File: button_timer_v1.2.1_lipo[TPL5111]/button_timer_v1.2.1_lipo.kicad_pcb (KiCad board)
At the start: 2 copper layers, 21 x 41.7 mm, 23 parts, among them J1 Conn_01x05_Female, SW1 SW_Push, SW2 SW_Push, U2 AP2112K-3.3, U3 TPL5111, X1 ESP-12E

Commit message: 3D Models etwas verbessert
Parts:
- C5: footprint Capacitor_SMD:C_0805_2012Metric_Pad1.18x1.45mm_HandSolder -> handsolder:C_0402_1005Metric_Pad0.74x0.62mm_HandSoldermod
- J1: footprint Connector_PinHeader_2.54mm:PinHeader_1x05_P2.54mm_Vertical -> Connector_PinSocket_2.54mm:PinSocket_1x05_P2.54mm_Vertical
- SW1: footprint Button_Switch_THT:SW_PUSH_6mm -> Button_Switch_THT:SW_PUSH_6mm_H8mm
- SW2: footprint Button_Switch_SMD:SW_SPST_EVQPE1 -> Button_Switch_SMD:SW_SPST_B3U-1000P
- moved C5 0.23 mm to (123.2, 64.0)
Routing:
- net Net-(BT1-Pad1): track 26.7 -> 18.7 mm
- net /GND: track 96.8 -> 97.4 mm

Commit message: Silkscreen Update
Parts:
- D2: footprint LED_SMD:LED_0805_2012Metric_Castellated -> handsolder:LED_0805_2012Metric_Castellated_mod

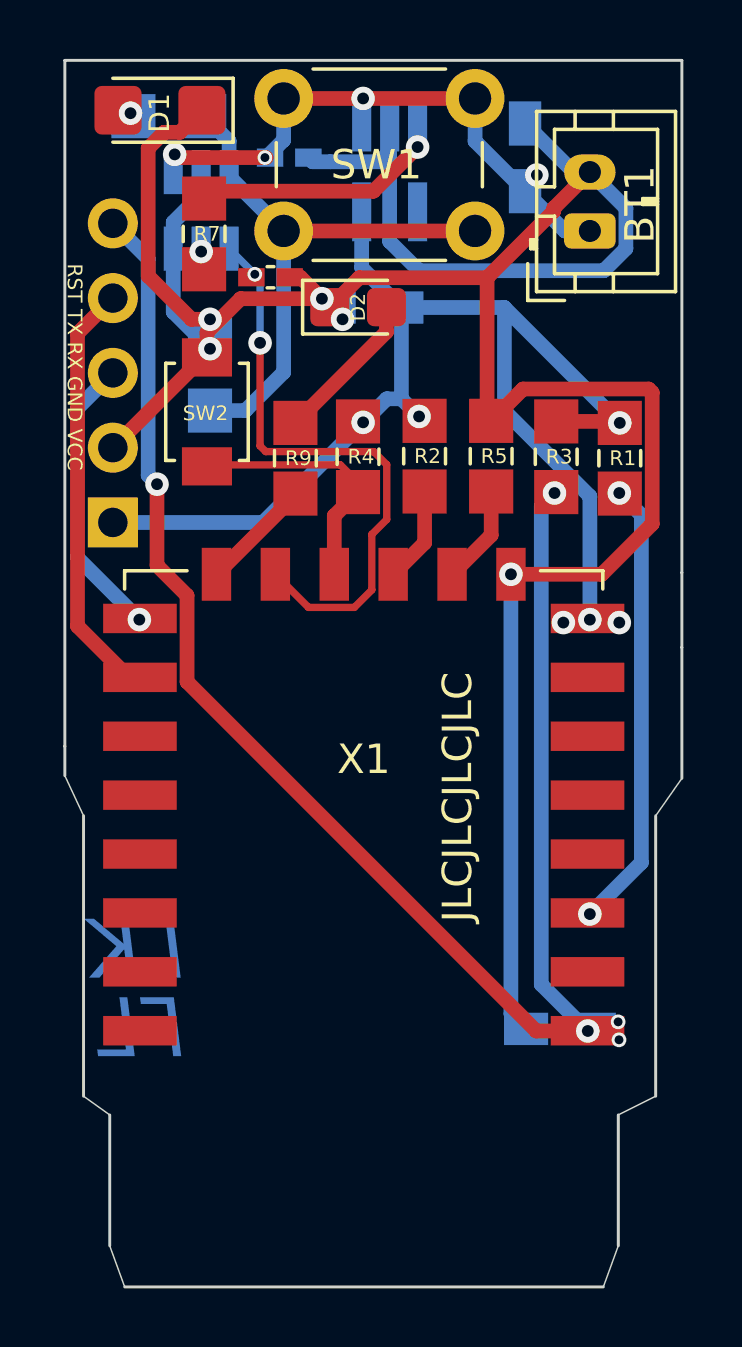
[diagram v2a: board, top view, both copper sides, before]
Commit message: cap between esp vcc and ground added
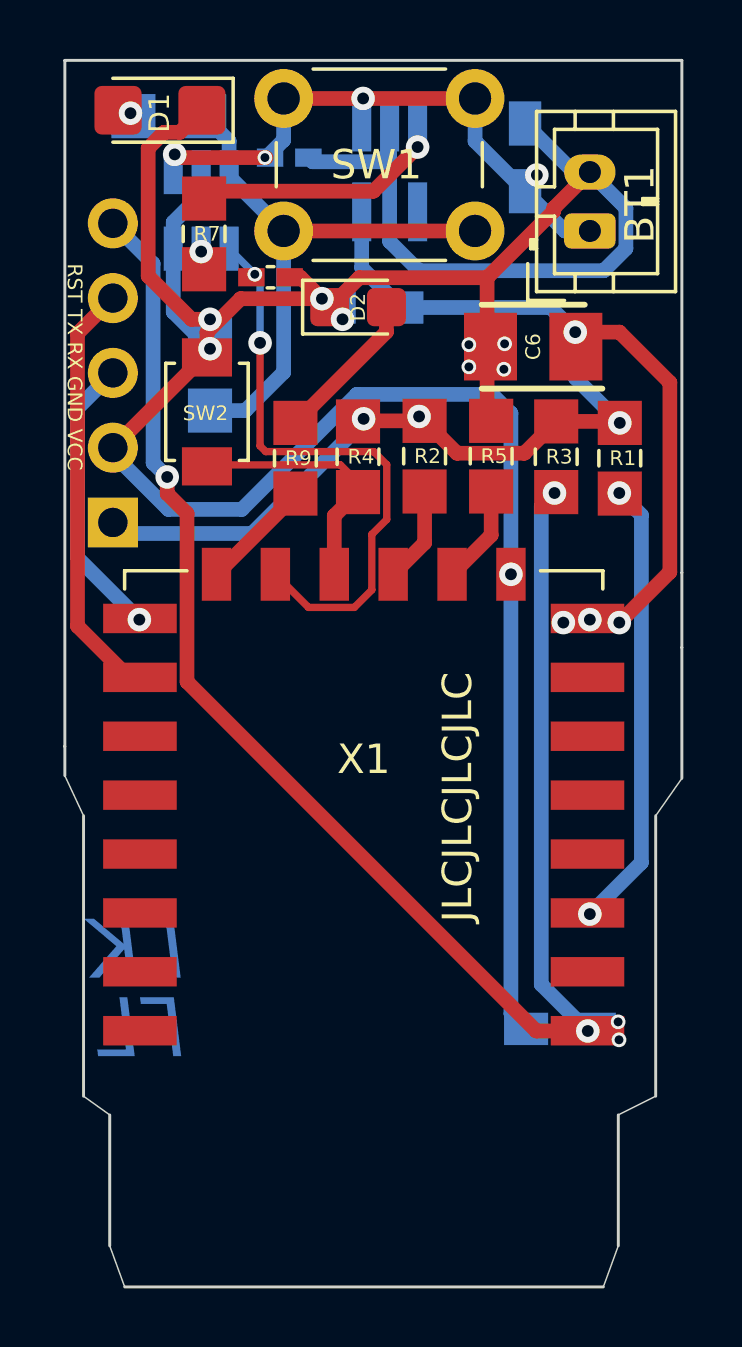
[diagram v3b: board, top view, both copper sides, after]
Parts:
- added C6: TAJB476M010TNJ, SamacSys_Parts:CAPPM3528X210N, F.Cu at (131.5, 70.4)
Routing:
- net /GND: track 97.4 -> 103.3 mm, vias 5 -> 9
- net /VCC: track 42.3 -> 46.5 mm, vias 6 -> 7

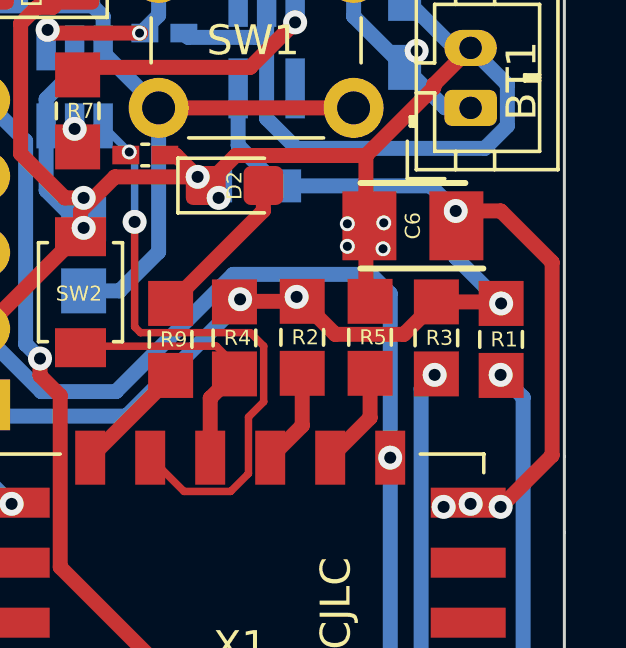
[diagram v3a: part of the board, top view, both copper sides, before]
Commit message: Added 100nF decoupling capacitors between VCC and Ground of the ESP
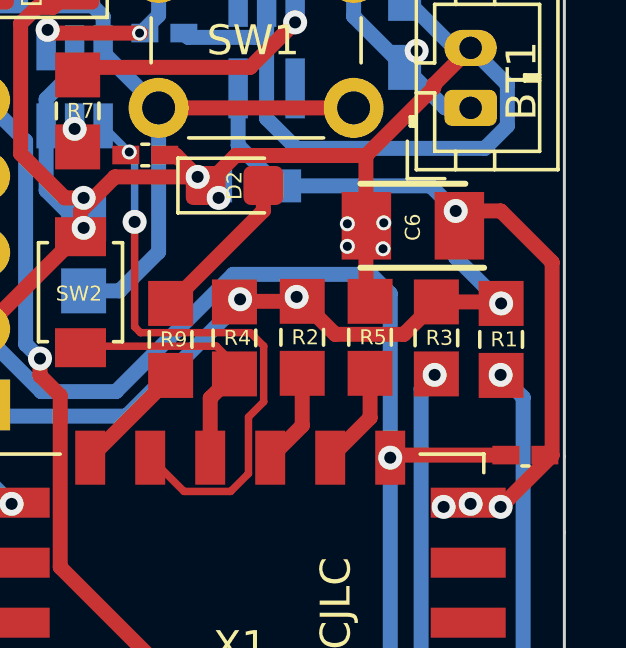
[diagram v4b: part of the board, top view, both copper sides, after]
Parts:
- added C7: 100nF, handsolder:C_0402_1005Metric_Pad0.74x0.62mm_HandSoldermod, F.Cu at (135.2, 78.1)
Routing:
- net /GND: track 103.3 -> 107.2 mm
